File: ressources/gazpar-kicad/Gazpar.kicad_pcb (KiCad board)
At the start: 2 copper layers, 44.4 x 59.1 mm, 7 parts, among them U1 PC817, U2 ESP32-DEVKITC-32D

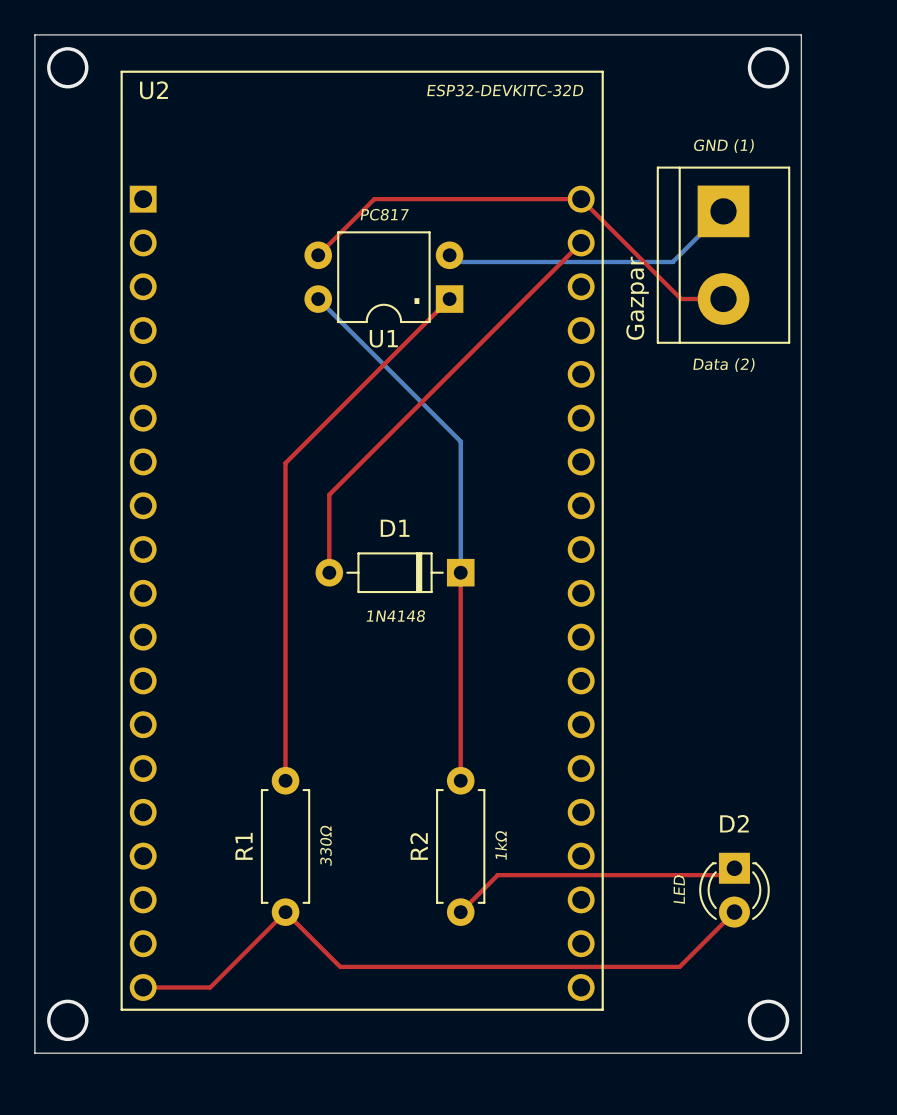
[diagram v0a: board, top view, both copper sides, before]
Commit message: Monocouche, fichiers de production, kibot, nomenclature, ...
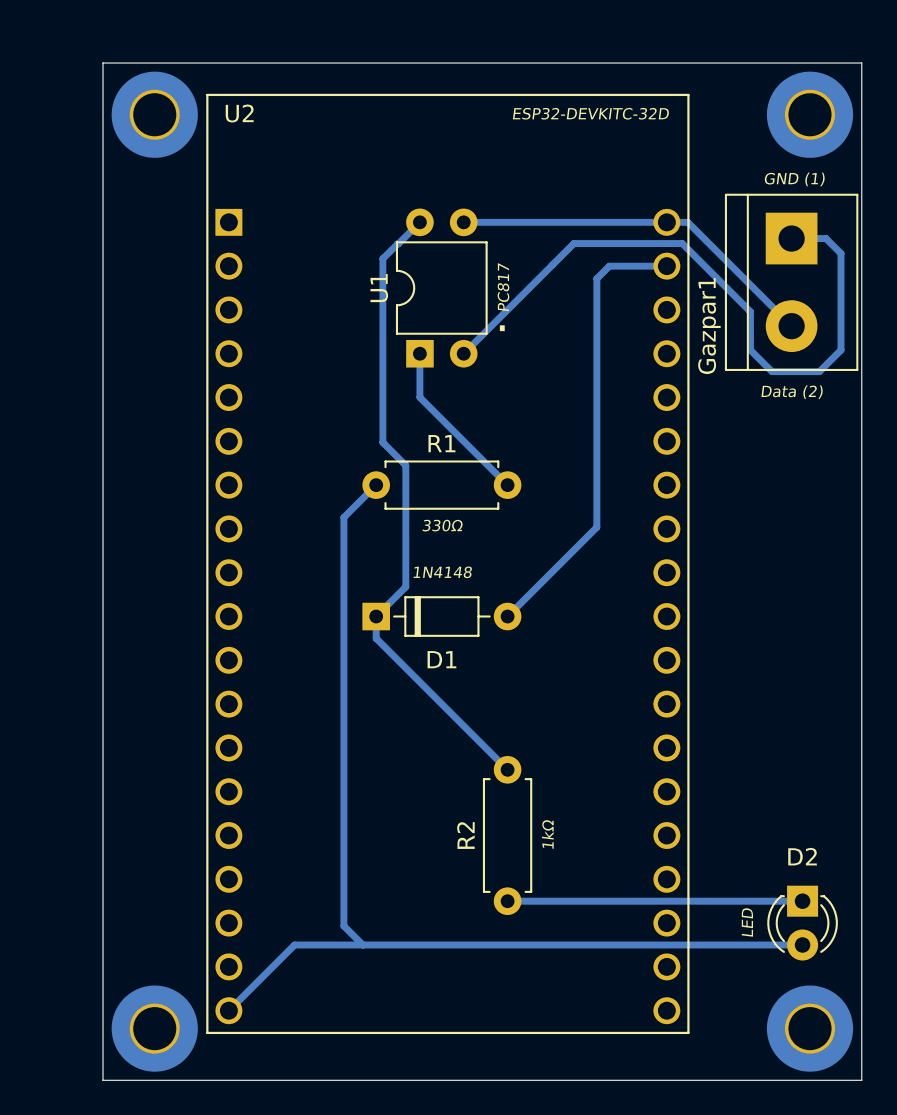
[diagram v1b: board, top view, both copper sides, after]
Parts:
- added H1: MountingHole_2.5mm_Pad_TopOnly, MountingHole:MountingHole_2.5mm_Pad_TopOnly, B.Cu at (153.0, 97.0)
- added H2: MountingHole_2.5mm_Pad_TopOnly, MountingHole:MountingHole_2.5mm_Pad_TopOnly, B.Cu at (191.0, 97.0)
- added H3: MountingHole_2.5mm_Pad_TopOnly, MountingHole:MountingHole_2.5mm_Pad_TopOnly, B.Cu at (191.0, 44.0)
- added H4: MountingHole_2.5mm_Pad_TopOnly, MountingHole:MountingHole_2.5mm_Pad_TopOnly, B.Cu at (153.0, 44.0)
- moved R1 25.3 mm to (165.8, 65.5), turned to 0 degrees
- moved D1 5.52 mm to (165.8, 73.1), turned to 0 degrees
- moved U2 5.15 mm to (170.0, 70.0)
- moved D2 4.39 mm to (190.6, 89.6)
- moved Gazpar1 4.25 mm to (189.9, 51.2)
- moved U1 3.61 mm to (168.4, 57.9), turned to 90 degrees
- moved R2 2.79 mm to (173.5, 89.6)
- renumbered Gazpar to Gazpar1
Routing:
- net Net-(D2-Pad2): track 38.7 -> 62.7 mm
- net Net-(R1-Pad2): track 31.9 -> 9.73 mm
- net Net-(Gazpar1-Pad1): track 17.3 -> 38.3 mm
- net Net-(Gazpar1-Pad2): track 27.3 -> 21.5 mm
- net Net-(D1-Pad1): track 31.4 -> 37.1 mm
- net Net-(D1-Pad2): track 25.2 -> 26.1 mm
- net (no net): vias 4 -> 0
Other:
- board size 44.4 x 59.1 mm -> 44 x 59 mm
